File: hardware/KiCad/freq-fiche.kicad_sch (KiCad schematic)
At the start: 24 parts, among them J1 Barrel_Jack_Switch_Pin3Ring, J2 AudioJack2, J3 AudioJack2, SW1 SW_SPST, SW2 SW_SPST, SW3 SW_SPDT, U1 LM7805_TO220, U2 Opamp_Dual

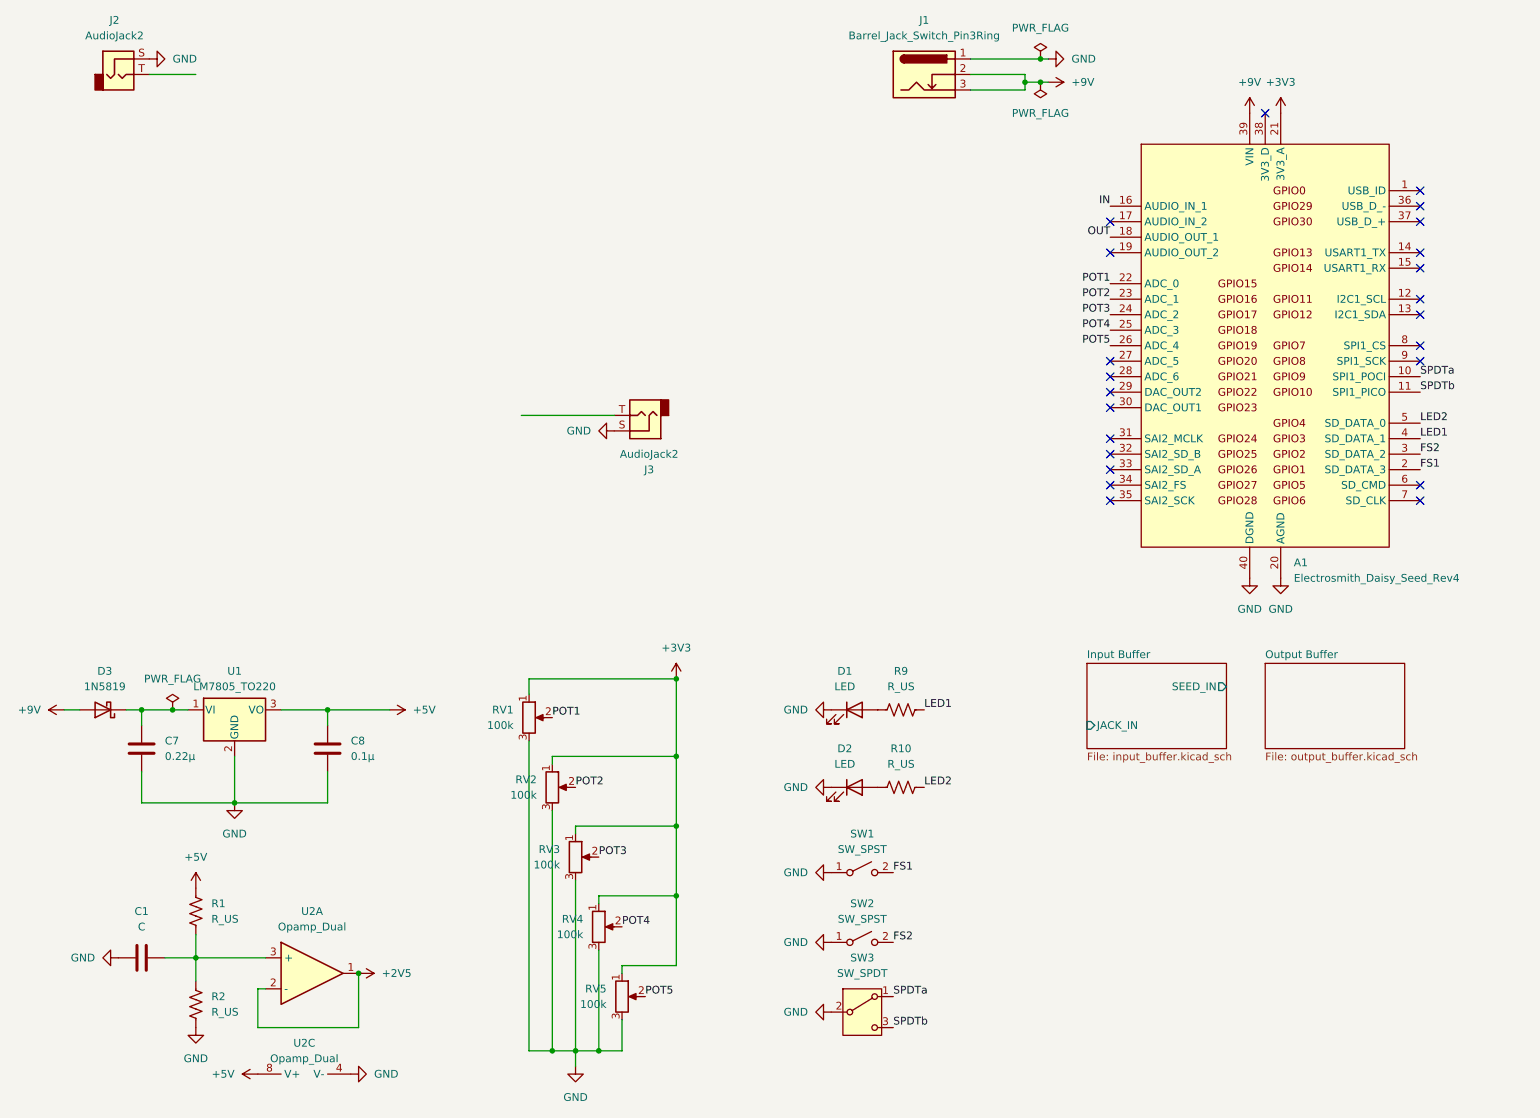
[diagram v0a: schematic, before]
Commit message: KiCad schematics on +3V3 single-supply.
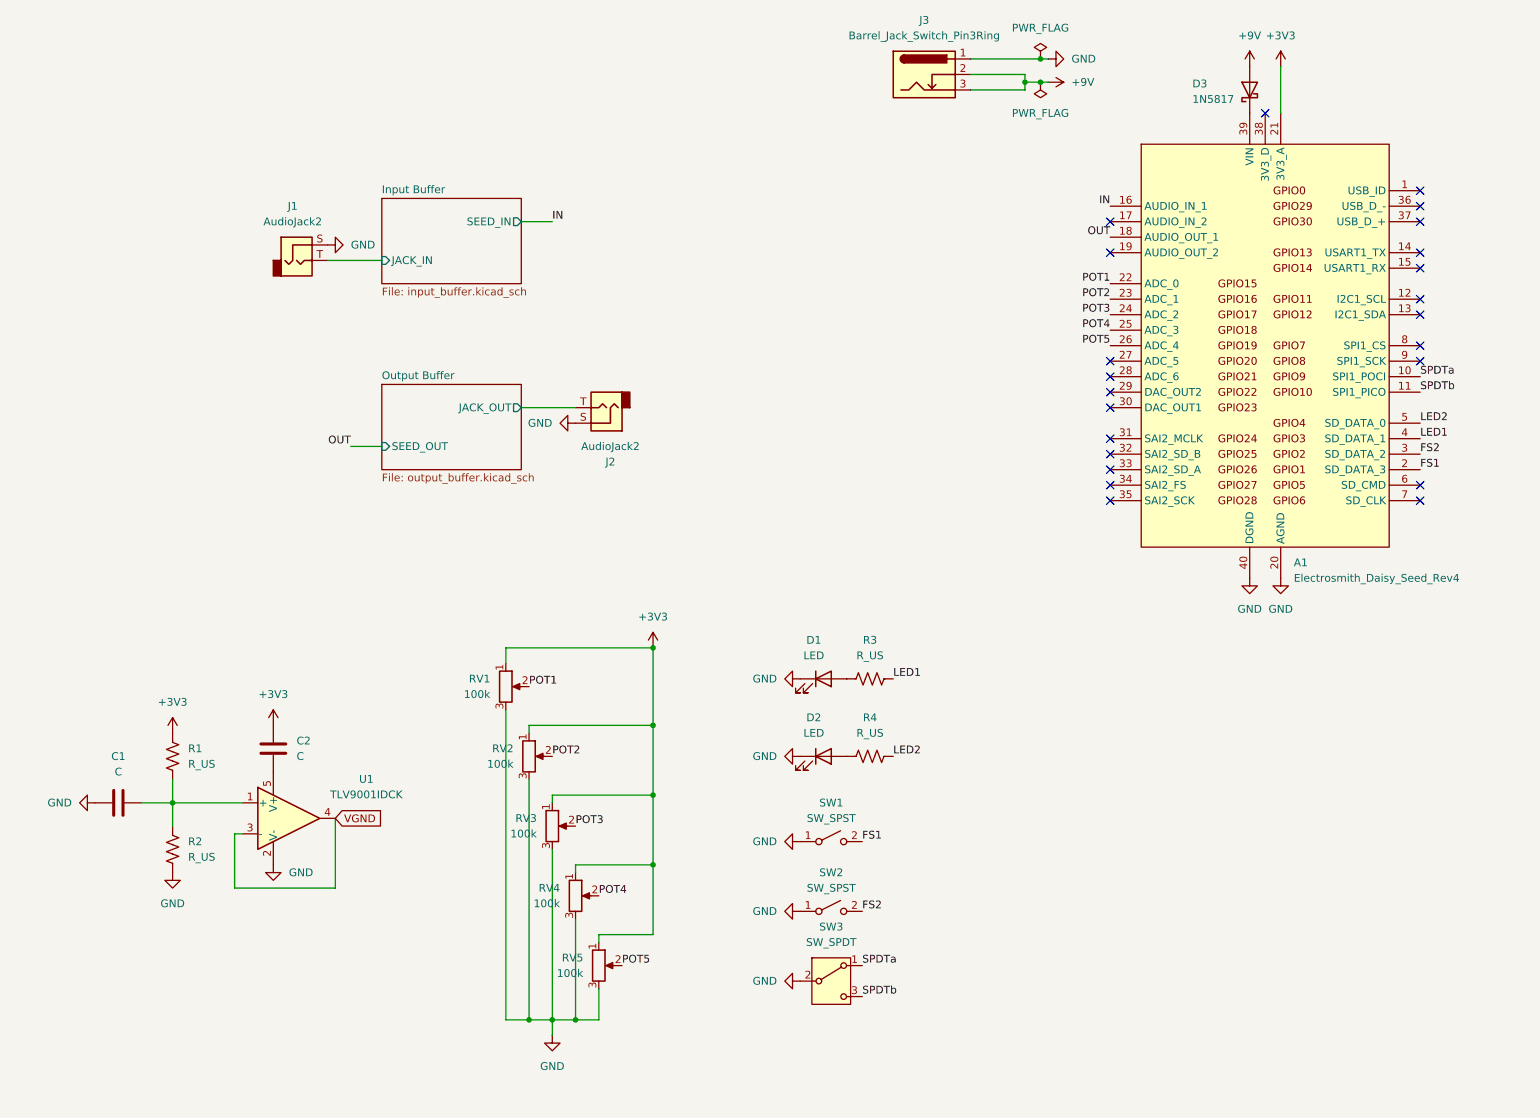
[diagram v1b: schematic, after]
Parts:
- removed C7: 0.22μ, symbol Device:C
- removed C8: 0.1μ, symbol Device:C
- removed D3: 1N5819, Diode_THT:D_DO-41_SOD81_P10.16mm_Horizontal, symbol Diode:1N5819
- removed U1: LM7805_TO220, Package_TO_SOT_THT:TO-220-3_Vertical, symbol Regulator_Linear:LM7805_TO220
- removed U2: Opamp_Dual, symbol Device:Opamp_Dual
- added C2: C, symbol Device:C
- added D3: 1N5817, Diode_THT:D_DO-41_SOD81_P10.16mm_Horizontal, symbol Diode:1N5817
- added U1: TLV9001IDCK, Package_TO_SOT_SMD:SOT-353_SC-70-5, symbol Amplifier_Operational:TLV9001IDCK
- renumbered J2 to J1, J3 to J2, J1 to J3, R9 to R3, R10 to R4
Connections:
- net +5V is gone; now on net +3V3: R1.1
- net +3V3: now also C2.1
- net +9V: now also D3.2 (A); no longer A1.39 (VIN)
- net GND: now also U1.2 (V-)
- net Input Buffer/JACK_IN: now also J1.T
- net at C1.2, R1.2, R2.1: now also U1.1 (+)
- net Output Buffer/JACK_OUT: now reaches J2.T
- new net: C2.2, U1.5 (V+)
- new net: A1.39 (VIN), D3.1 (K)
- new net VGND: U1.3 (-), U1.4
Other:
- sheet Output Buffer ports: added JACK_OUT, SEED_OUT; removed none
- moved on the sheet: C1, D1, D2, J1, J2, R1, R2, R3, R4, RV1, RV2, RV3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

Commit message: Input buffer simplification; removal of BAS70-04 diodes.
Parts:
- C1: value C -> 1µ
- C2: value C -> 0µ1
- R1, R2: value R_US -> 100k
- R3, R4: value R_US -> 1k

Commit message: DC bias coupling cap.
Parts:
- C1: value 1µ -> 0µ1
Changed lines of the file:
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@@
 			)
 		)
-		(property "Value" "1µ"
+		(property "Value" "0µ1"
 			(at 38.1 140.97 90)
 			(show_name no)

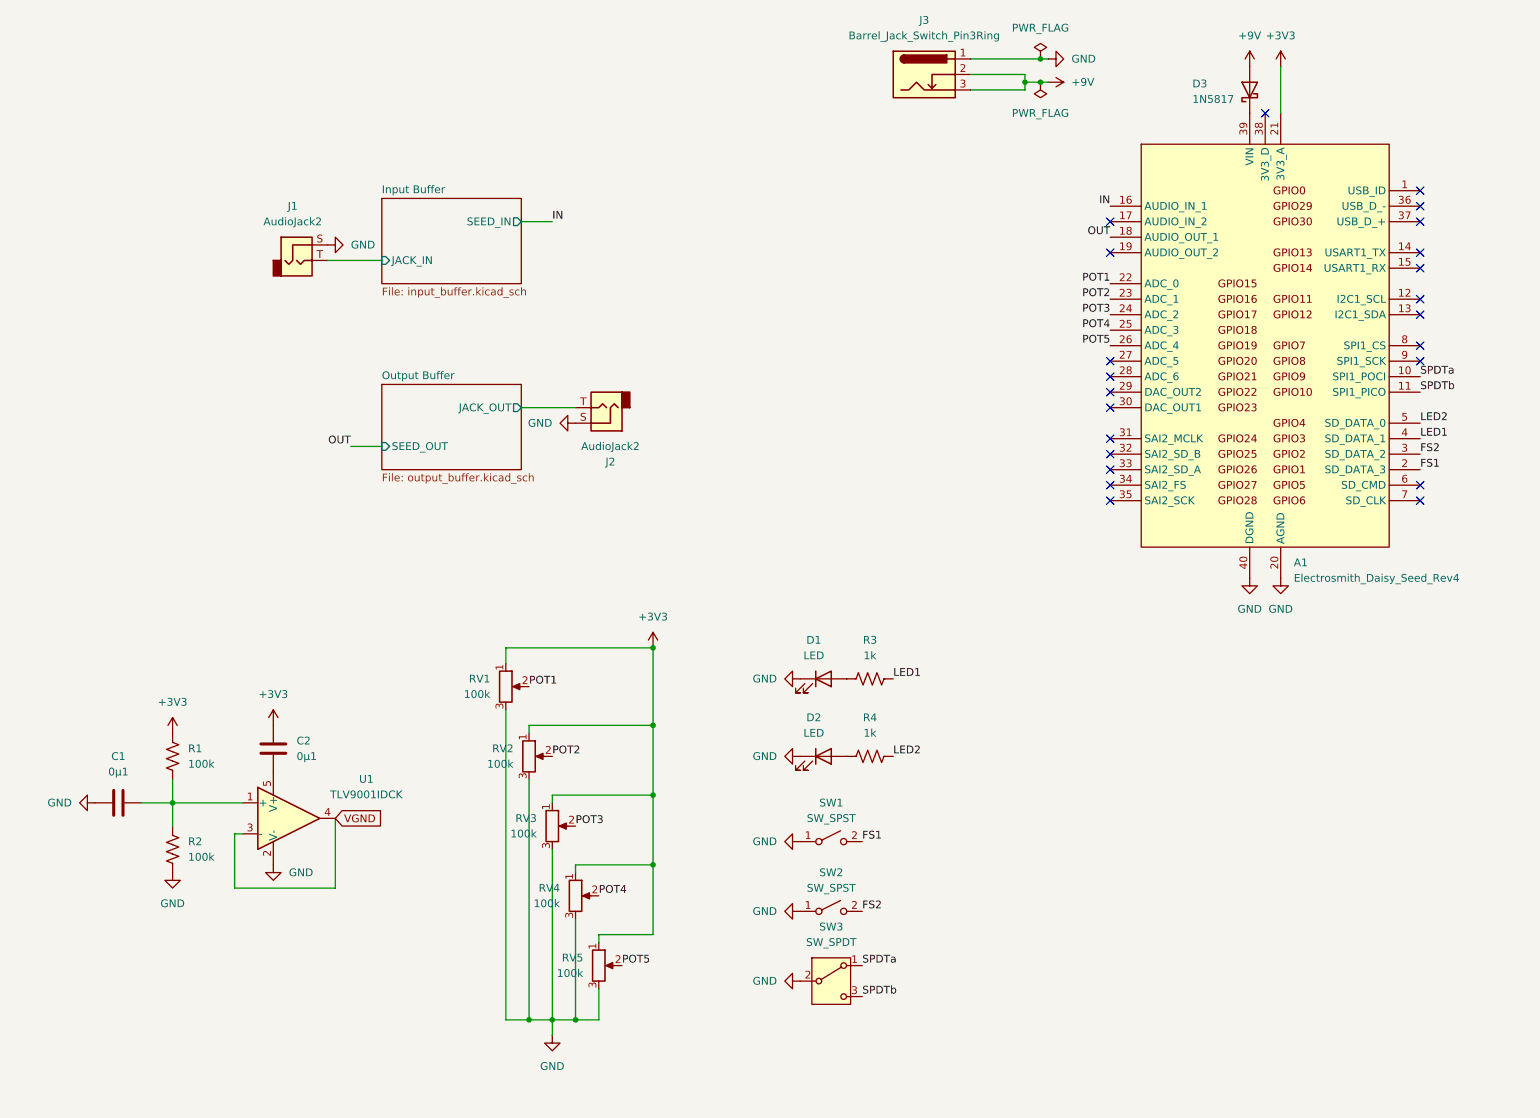
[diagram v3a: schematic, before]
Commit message: Reduction in number of op amps from 5 to 4.
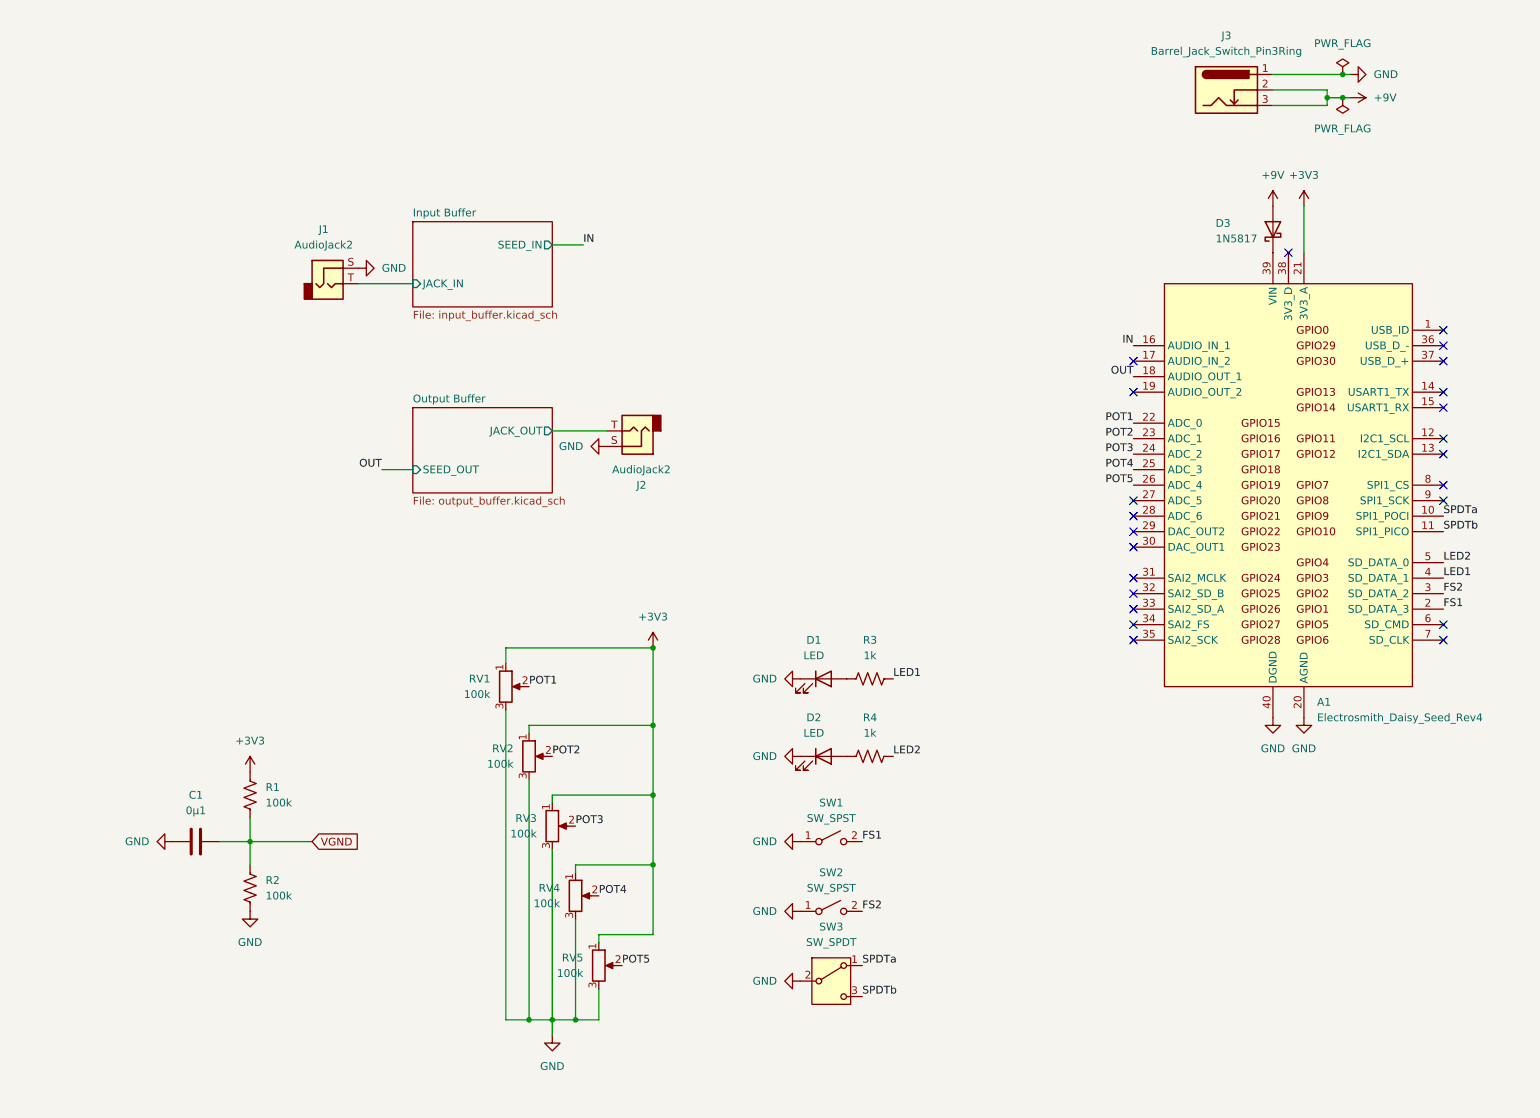
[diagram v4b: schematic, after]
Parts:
- removed C2: 0µ1, symbol Device:C
- removed U1: TLV9001IDCK, Package_TO_SOT_SMD:SOT-353_SC-70-5, symbol Amplifier_Operational:TLV9001IDCK
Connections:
- net VGND: now also C1.2, R1.2, R2.1
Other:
- moved on the sheet: A1, C1, D3, J1, J2, J3, R1, R2
